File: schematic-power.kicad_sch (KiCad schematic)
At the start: 32 parts, among them U4 TPS62933, U9 TPS62933

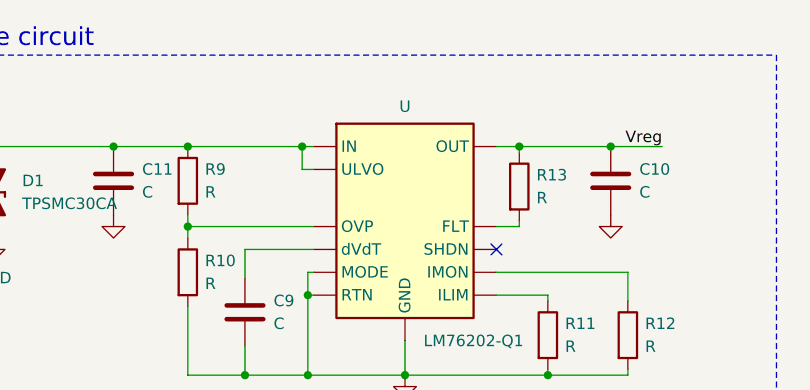
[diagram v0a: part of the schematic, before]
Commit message: Rename project files and setup crystal oscillator
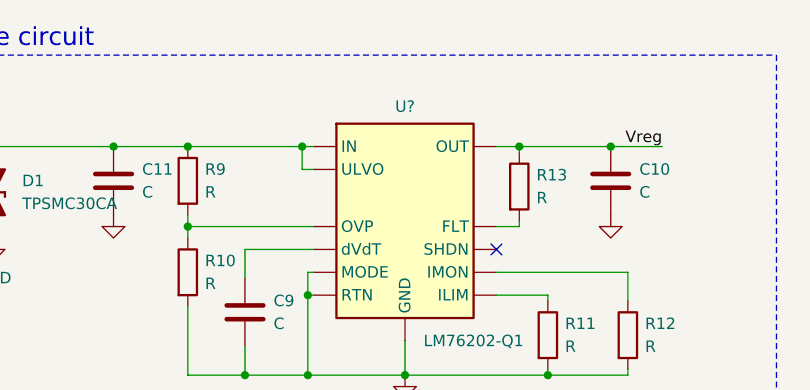
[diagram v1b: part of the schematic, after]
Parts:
- renumbered U to U?

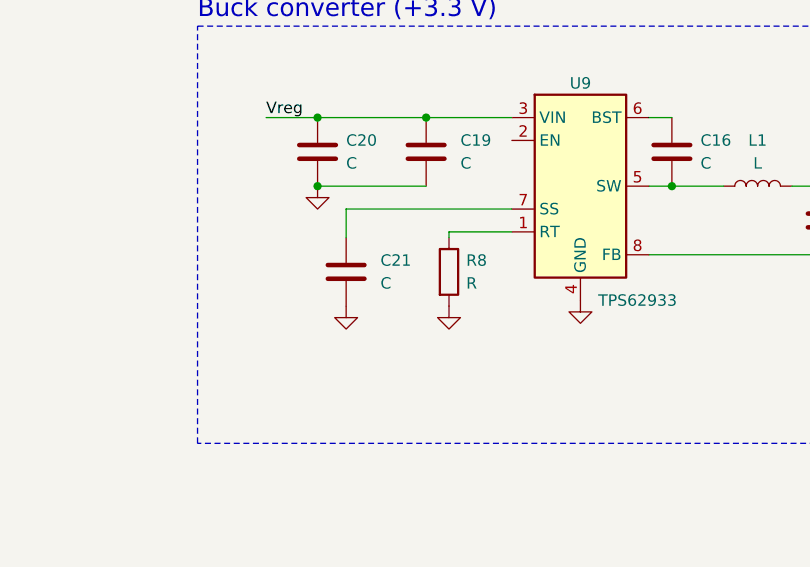
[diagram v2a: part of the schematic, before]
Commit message: Add capacitor value
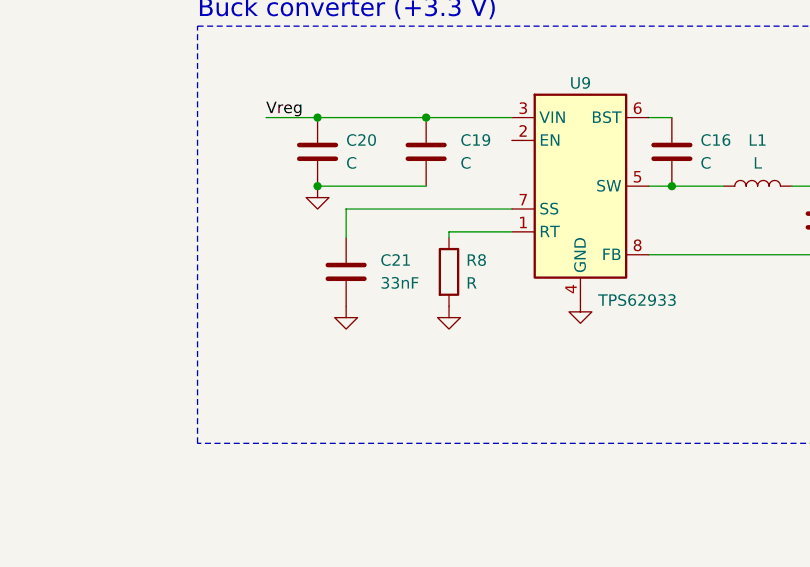
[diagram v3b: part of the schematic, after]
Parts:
- C21: value C -> 33nF
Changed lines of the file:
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@@
       (effects (font (size 1.27 1.27)) (justify left))
     )
-    (property "Value" "C" (at 170.18 138.4299 0)
+    (property "Value" "33nF" (at 170.18 138.4299 0)
       (effects (font (size 1.27 1.27)) (justify left))
     )

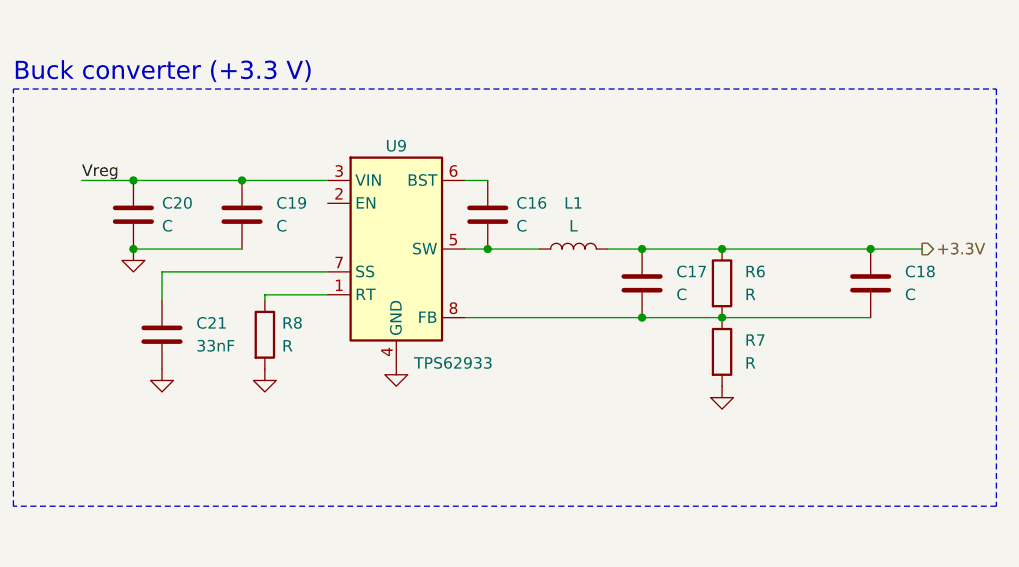
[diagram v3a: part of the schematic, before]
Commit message: Add values for buck converter 3,3V
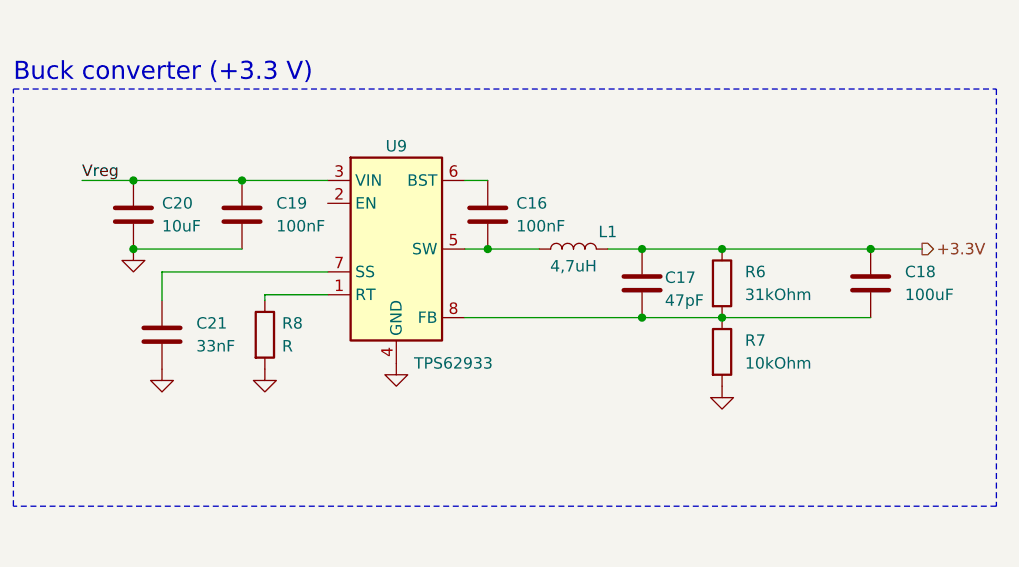
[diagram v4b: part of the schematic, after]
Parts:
- C16, C19: value C -> 100nF
- C17: value C -> 47pF
- C18: value C -> 100uF
- C20: value C -> 10uF
- L1: value L -> 4,7uH
- R6: value R -> 31kOhm
- R7: value R -> 10kOhm
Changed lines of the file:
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@@
   (symbol (lib_id "Device:C") (at 202.565 123.825 0) (unit 1)
     (in_bom yes) (on_board yes) (dnp no) (fields_autoplaced)
-    (property "Reference" "C16" (at 205.74 122.5549 0)
-      (effects (font (size 1.27 1.27)) (justify left))
-    )
-    (property "Value" "C" (at 205.74 125.0949 0)
+    (property "Reference" "C16" (at 205.74 122.555 0)
+      (effects (font (size 1.27 1.27)) (justify left))
+    )
+    (property "Value" "100nF" (at 205.74 125.095 0)
       (effects (font (size 1.27 1.27)) (justify left))
     )
@@
   )
   (symbol (lib_id "Device:L") (at 212.09 127.635 90) (unit 1)
-    (in_bom yes) (on_board yes) (dnp no) (fields_autoplaced)
-    (property "Reference" "L1" (at 212.09 122.555 90)
+    (in_bom yes) (on_board yes) (dnp no)
+    (property "Reference" "L1" (at 215.9 125.73 90)
       (effects (font (size 1.27 1.27)))
     )
-    (property "Value" "L" (at 212.09 125.095 90)
+    (property "Value" "4,7uH" (at 212.09 129.54 90)
       (effects (font (size 1.27 1.27)))
     )
@@
   (symbol (lib_id "Device:R") (at 228.6 131.445 0) (unit 1)
     (in_bom yes) (on_board yes) (dnp no) (fields_autoplaced)
-    (property "Reference" "R6" (at 231.14 130.1749 0)
-      (effects (font (size 1.27 1.27)) (justify left))
-    )
-    (property "Value" "R" (at 231.14 132.7149 0)
+    (property "Reference" "R6" (at 231.14 130.175 0)
+      (effects (font (size 1.27 1.27)) (justify left))
+    )
+    (property "Value" "31kOhm" (at 231.14 132.715 0)
       (effects (font (size 1.27 1.27)) (justify left))
     )
@@
   )
   (symbol (lib_id "Device:C") (at 219.71 131.445 0) (unit 1)
-    (in_bom yes) (on_board yes) (dnp no) (fields_autoplaced)
-    (property "Reference" "C17" (at 223.52 130.1749 0)
-      (effects (font (size 1.27 1.27)) (justify left))
-    )
-    (property "Value" "C" (at 223.52 132.7149 0)
+    (in_bom yes) (on_board yes) (dnp no)
+    (property "Reference" "C17" (at 222.25 130.81 0)
+      (effects (font (size 1.27 1.27)) (justify left))
+    )
+    (property "Value" "47pF" (at 222.25 133.35 0)
       (effects (font (size 1.27 1.27)) (justify left))
     )
@@
       (effects (font (size 1.27 1.27)) (justify left))
     )
-    (property "Value" "C" (at 166.37 125.0949 0)
+    (property "Value" "10uF" (at 166.37 125.0949 0)
       (effects (font (size 1.27 1.27)) (justify left))
     )
@@
   (symbol (lib_id "Device:C") (at 245.11 131.445 0) (unit 1)
     (in_bom yes) (on_board yes) (dnp no) (fields_autoplaced)
-    (property "Reference" "C18" (at 248.92 130.1749 0)
-      (effects (font (size 1.27 1.27)) (justify left))
-    )
-    (property "Value" "C" (at 248.92 132.7149 0)
+    (property "Reference" "C18" (at 248.92 130.175 0)
+      (effects (font (size 1.27 1.27)) (justify left))
+    )
+    (property "Value" "100uF" (at 248.92 132.715 0)
       (effects (font (size 1.27 1.27)) (justify left))
     )
@@
   (symbol (lib_id "Device:C") (at 175.26 123.825 0) (unit 1)
     (in_bom yes) (on_board yes) (dnp no) (fields_autoplaced)
-    (property "Reference" "C19" (at 179.07 122.5549 0)
-      (effects (font (size 1.27 1.27)) (justify left))
-    )
-    (property "Value" "C" (at 179.07 125.0949 0)
+    (property "Reference" "C19" (at 179.07 122.555 0)
+      (effects (font (size 1.27 1.27)) (justify left))
+    )
+    (property "Value" "100nF" (at 179.07 125.095 0)
       (effects (font (size 1.27 1.27)) (justify left))
     )
@@
   (symbol (lib_id "Device:R") (at 228.6 139.065 0) (unit 1)
     (in_bom yes) (on_board yes) (dnp no) (fields_autoplaced)
-    (property "Reference" "R7" (at 231.14 137.7949 0)
-      (effects (font (size 1.27 1.27)) (justify left))
-    )
-    (property "Value" "R" (at 231.14 140.3349 0)
-      (effects (font (size 1.27 1.27)) (justify left))
-    )
+    (property "Reference" "R7" (at 231.14 137.795 0)
+      (effects (font (size 1.27 1.27)) (justify left))
+    )
+    (property "Value" "10kOhm" (at 231.14 140.335 0)
+      (effects (font (size 1.27 1.27)) (justify left))
+    )

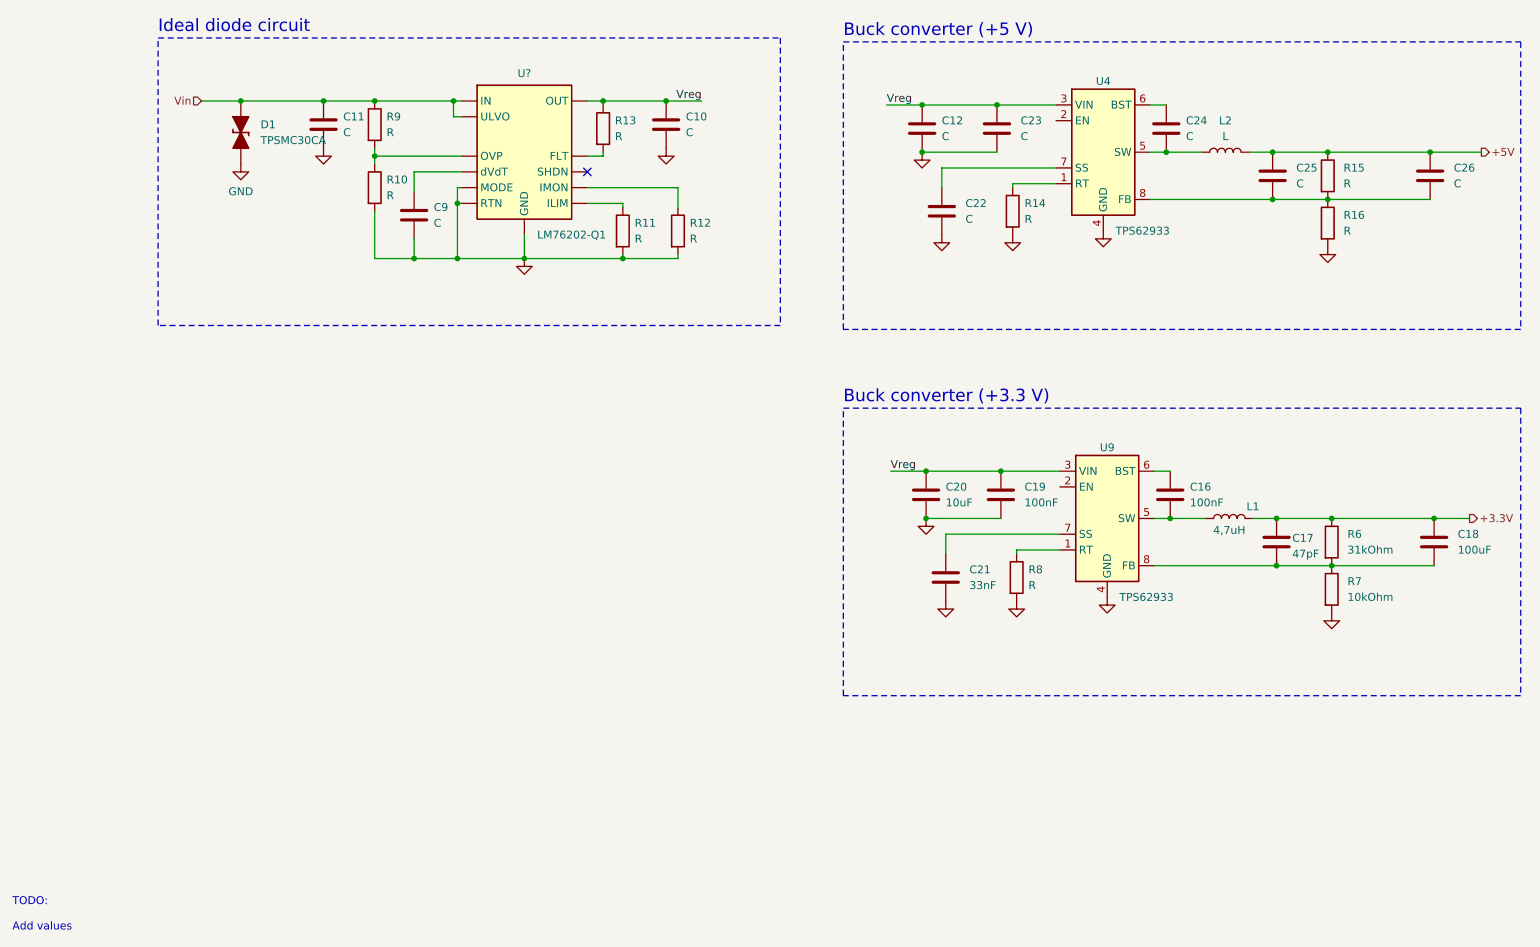
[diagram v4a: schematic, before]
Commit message: Add values for buck converter 5V
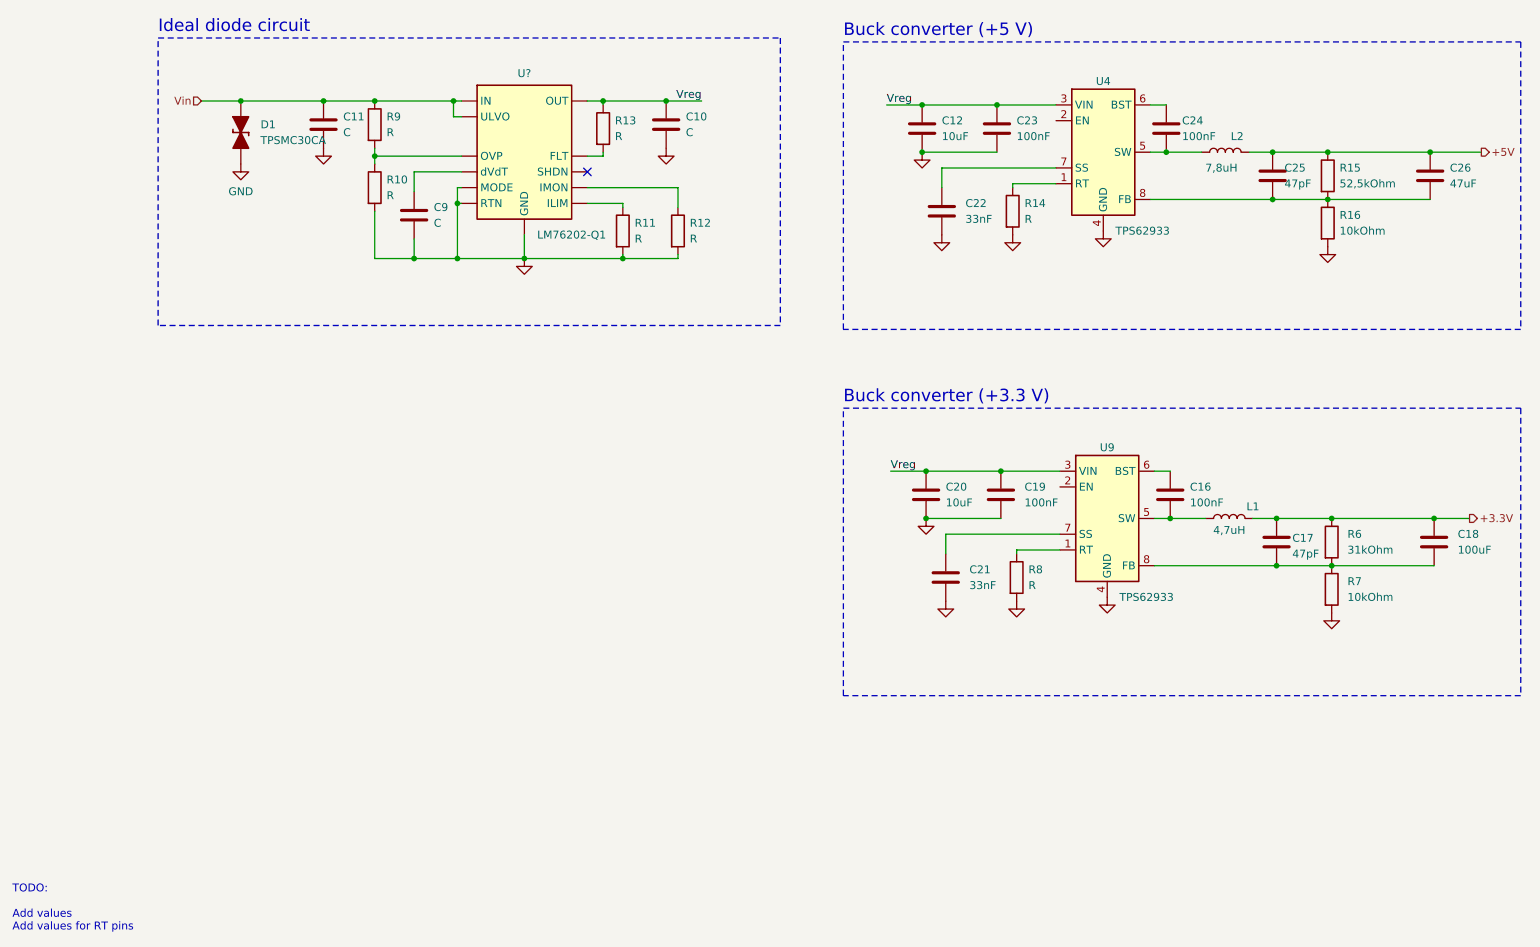
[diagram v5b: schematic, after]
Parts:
- C12: value C -> 10uF
- C22: value C -> 33nF
- C23, C24: value C -> 100nF
- C25: value C -> 47pF
- C26: value C -> 47uF
- L2: value L -> 7,8uH
- R15: value R -> 52,5kOhm
- R16: value R -> 10kOhm
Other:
- note added: "TODO: Add values Add values for RT pins"
- note removed: "TODO: Add values"
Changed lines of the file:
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@@
     (effects (font (size 2 2)) (justify left bottom))
   )
-  (text "TODO:\n\nAdd values" (at 15.875 194.31 0)
+  (text "TODO:\n\nAdd values \nAdd values for RT pins" (at 15.875 194.31 0)
     (effects (font (size 1.27 1.27)) (justify left bottom))
   )
@@
       (effects (font (size 1.27 1.27)) (justify left))
     )
-    (property "Value" "C" (at 169.545 79.3749 0)
+    (property "Value" "33nF" (at 169.545 79.3749 0)
       (effects (font (size 1.27 1.27)) (justify left))
     )
@@
   (symbol (lib_id "Device:C") (at 174.625 64.77 0) (unit 1)
     (in_bom yes) (on_board yes) (dnp no) (fields_autoplaced)
-    (property "Reference" "C23" (at 178.435 63.4999 0)
-      (effects (font (size 1.27 1.27)) (justify left))
-    )
-    (property "Value" "C" (at 178.435 66.0399 0)
+    (property "Reference" "C23" (at 177.8 63.5 0)
+      (effects (font (size 1.27 1.27)) (justify left))
+    )
+    (property "Value" "100nF" (at 177.8 66.04 0)
       (effects (font (size 1.27 1.27)) (justify left))
     )
@@
       (effects (font (size 1.27 1.27)) (justify left))
     )
-    (property "Value" "C" (at 165.735 66.0399 0)
+    (property "Value" "10uF" (at 165.735 66.0399 0)
       (effects (font (size 1.27 1.27)) (justify left))
     )
@@
   )
   (symbol (lib_id "Device:C") (at 219.075 72.39 0) (unit 1)
-    (in_bom yes) (on_board yes) (dnp no) (fields_autoplaced)
-    (property "Reference" "C25" (at 222.885 71.1199 0)
-      (effects (font (size 1.27 1.27)) (justify left))
-    )
-    (property "Value" "C" (at 222.885 73.6599 0)
+    (in_bom yes) (on_board yes) (dnp no)
+    (property "Reference" "C25" (at 220.98 71.12 0)
+      (effects (font (size 1.27 1.27)) (justify left))
+    )
+    (property "Value" "47pF" (at 220.98 73.66 0)
       (effects (font (size 1.27 1.27)) (justify left))
     )
@@
   (symbol (lib_id "Device:R") (at 227.965 80.01 0) (unit 1)
     (in_bom yes) (on_board yes) (dnp no) (fields_autoplaced)
-    (property "Reference" "R16" (at 230.505 78.7399 0)
-      (effects (font (size 1.27 1.27)) (justify left))
-    )
-    (property "Value" "R" (at 230.505 81.2799 0)
+    (property "Reference" "R16" (at 229.87 78.74 0)
+      (effects (font (size 1.27 1.27)) (justify left))
+    )
+    (property "Value" "10kOhm" (at 229.87 81.28 0)
       (effects (font (size 1.27 1.27)) (justify left))
     )
@@
   )
   (symbol (lib_id "Device:L") (at 211.455 68.58 90) (unit 1)
-    (in_bom yes) (on_board yes) (dnp no) (fields_autoplaced)
-    (property "Reference" "L2" (at 211.455 63.5 90)
+    (in_bom yes) (on_board yes) (dnp no)
+    (property "Reference" "L2" (at 213.36 66.04 90)
       (effects (font (size 1.27 1.27)))
     )
-    (property "Value" "L" (at 211.455 66.04 90)
+    (property "Value" "7,8uH" (at 210.82 71.12 90)
       (effects (font (size 1.27 1.27)))
     )
@@
   (symbol (lib_id "Device:R") (at 227.965 72.39 0) (unit 1)
     (in_bom yes) (on_board yes) (dnp no) (fields_autoplaced)
-    (property "Reference" "R15" (at 230.505 71.1199 0)
-      (effects (font (size 1.27 1.27)) (justify left))
-    )
-    (property "Value" "R" (at 230.505 73.6599 0)
+    (property "Reference" "R15" (at 229.87 71.12 0)
+      (effects (font (size 1.27 1.27)) (justify left))
+    )
+    (property "Value" "52,5kOhm" (at 229.87 73.66 0)
       (effects (font (size 1.27 1.27)) (justify left))
     )
@@
   )
   (symbol (lib_id "Device:C") (at 201.93 64.77 0) (unit 1)
-    (in_bom yes) (on_board yes) (dnp no) (fields_autoplaced)
-    (property "Reference" "C24" (at 205.105 63.4999 0)
-      (effects (font (size 1.27 1.27)) (justify left))
-    )
-    (property "Value" "C" (at 205.105 66.0399 0)
+    (in_bom yes) (on_board yes) (dnp no)
+    (property "Reference" "C24" (at 204.47 63.5 0)
+      (effects (font (size 1.27 1.27)) (justify left))
+    )
+    (property "Value" "100nF" (at 204.47 66.04 0)
       (effects (font (size 1.27 1.27)) (justify left))
     )
@@
   (symbol (lib_id "Device:C") (at 244.475 72.39 0) (unit 1)
     (in_bom yes) (on_board yes) (dnp no) (fields_autoplaced)
-    (property "Reference" "C26" (at 248.285 71.1199 0)
-      (effects (font (size 1.27 1.27)) (justify left))
-    )
-    (property "Value" "C" (at 248.285 73.6599 0)
-      (effects (font (size 1.27 1.27)) (justify left))
-    )
+    (property "Reference" "C26" (at 247.65 71.12 0)
+      (effects (font (size 1.27 1.27)) (justify left))
+    )
+    (property "Value" "47uF" (at 247.65 73.66 0)
+      (effects (font (size 1.27 1.27)) (justify left))
+    )
